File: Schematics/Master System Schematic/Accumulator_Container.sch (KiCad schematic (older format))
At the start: 21 parts, among them J10 Main TS Connector, J11 TSAL Connector, J8 Shutdown/MC Control Connector, J9 TSMP/IMD Connector, K10 SPST-NO (Precharge Control), K11 SPST-NC (Discharge), K12 SPST-NO (AIR Control), K7 SPST-NO (Precharge), K8 SPST-NO (AIR), K9 SPST-NO (AIR), U14 OrionCurrentSens, U7 OrionThermExp

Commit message: Cleaned accumulator
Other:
- moved on the sheet: F6, F7, F8, F9, J10, J11, J9, K11, K7, K8, K9, R2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

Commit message: Revert "Revert "Merge branch 'Dylan_BMS-control-systems-slight-rework' of https://github.com/Northeastern-Electric-Racing/NER into Dylan_BMS-control-systems-slight-rework""
This reverts commit 7bfceb9de4e286d5e46c7b991145f3115c617458.
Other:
- note added: "Contains 4 critical thermistors, 4 critical thermistor gnds, thermistor expansion pwr and gnd, and thermistor expansion CANBUS"
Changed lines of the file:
@@
 Sheet 3 23
 Title "Accumulator Container"
-Date "2020-11-12"
-Rev "6"
+Date "2021-02-08"
+Rev "7"
 Comp "Northeastern Electric Racing"
 Comment1 "https://github.com/Northeastern-Electric-Racing/NER"
@@
 NoConn ~ 2750 1800
 NoConn ~ 4150 1500
-Text HLabel 19650 14600 2    50   Output ~ 0
-Segment1_CriticalThermistors
-Text HLabel 19650 14700 2    50   Output ~ 0
-Segment2_CriticalThermistors
-Text HLabel 19650 14800 2    50   Output ~ 0
-Segment3_CriticalThermistors
-Text HLabel 19650 14900 2    50   Output ~ 0
-Segment4_CriticalThermistors
 Entry Wire Line
 	2350 2300 2250 2400
@@
 	2750 1600 2650 1600
 Text HLabel 19650 13450 2    50   Output ~ 0
-Thermistor_Expansion
+Temperature_Data
 Entry Wire Line
 	2550 1800 2650 1900
@@
 	2650 15900 4150 15900
 Wire Bus Line
-	1300 5150 600  5150
-Wire Bus Line
-	600  5150 600  16400
-Wire Bus Line
-	1300 8050 650  8050
-Wire Bus Line
-	650  8050 650  16300
-Wire Bus Line
-	1300 10950 700  10950
-Wire Bus Line
-	1300 13850 750  13850
-Wire Bus Line
-	750  13850 750  16100
-Wire Bus Line
-	700  10950 700  16200
+	1300 5150 750  5150
+Wire Bus Line
+	1300 8050 700  8050
+Wire Bus Line
+	1300 10950 650  10950
 Wire Bus Line
 	1300 13750 800  13750
@@
 	10100 2150 10100 5600
 Wire Bus Line
-	600  16400 13650 16400
-Wire Bus Line
-	650  16300 13550 16300
-Wire Bus Line
-	700  16200 13450 16200
-Wire Bus Line
-	750  16100 13350 16100
-Wire Bus Line
-	13450 14700 19650 14700
-Wire Bus Line
 	19250 13450 19650 13450
 Wire Bus Line
@@
 Wire Notes Line
 	21100 15000 21100 13350
-Wire Bus Line
-	13650 14900 19650 14900
-Wire Bus Line
-	13550 14800 19650 14800
 Wire Notes Line
 	19450 13350 19450 15000
@@
 Wire Bus Line
 	10600 14300 19650 14300
-Wire Bus Line
-	13350 14600 19650 14600
 Connection ~ 11850 6950
 Wire Wire Line
@@
 	13850 3850 13850 5550
 Wire Bus Line
-	13650 14900 13650 16400
-Wire Bus Line
-	13550 14800 13550 16300
-Wire Bus Line
-	13450 14700 13450 16200
-Wire Bus Line
-	13350 14600 13350 16100
-Wire Bus Line
 	19250 11200 19250 13450
 Wire Bus Line
 	19100 11050 19100 13750
+Entry Bus Bus
+	650  850  750  750
+Wire Bus Line
+	650  10950 650  850
+Wire Bus Line
+	600  13850 600  850
+Wire Bus Line
+	600  13850 1300 13850
+Entry Bus Bus
+	600  850  700  750
+Entry Bus Bus
+	750  850  850  750
+Entry Bus Bus
+	700  850  800  750
+Wire Bus Line
+	700  850  700  8050
+Wire Bus Line
+	750  850  750  5150
 Wire Bus Line
 	10600 12200 10600 14200
@@
 	10700 6400 10700 14000
 Wire Bus Line
-	2650 750  20850 750
-Wire Bus Line
 	10600 14300 10600 15000
 Wire Bus Line
@@
 	18150 6300 20700 6300
 Wire Bus Line
+	700  750  20850 750
+Wire Bus Line
 	4400 3350 4400 4400
 Wire Bus Line
@@
 Wire Bus Line
 	2250 2300 2250 4300
+Text Notes 4500 850  0    50   ~ 0
+Contains 4 critical thermistors, 4 critical thermistor gnds, thermistor expansion pwr and gnd, and thermistor expansion CANBUS
 $EndSCHEMATC

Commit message: Revert "Merge branch 'Dylan_BMS-control-systems-slight-rework' of https://github.com/Northeastern-Electric-Racing/NER into Dylan_BMS-control-systems-slight-rework"
This reverts commit fde7ba4e4a38cad13224d6abfd117b52e4ba179f, reversing
changes made to 479d55be7c023c6502d2d4db07d9957a4b0a3a94.
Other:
- note removed: "Contains 4 critical thermistors, 4 critical thermistor gnds, thermistor expansion pwr and gnd, and thermistor expansion CANBUS"
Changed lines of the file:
@@
 Sheet 3 23
 Title "Accumulator Container"
-Date "2021-02-08"
-Rev "7"
+Date "2020-11-12"
+Rev "6"
 Comp "Northeastern Electric Racing"
 Comment1 "https://github.com/Northeastern-Electric-Racing/NER"
@@
 NoConn ~ 2750 1800
 NoConn ~ 4150 1500
+Text HLabel 19650 14600 2    50   Output ~ 0
+Segment1_CriticalThermistors
+Text HLabel 19650 14700 2    50   Output ~ 0
+Segment2_CriticalThermistors
+Text HLabel 19650 14800 2    50   Output ~ 0
+Segment3_CriticalThermistors
+Text HLabel 19650 14900 2    50   Output ~ 0
+Segment4_CriticalThermistors
 Entry Wire Line
 	2350 2300 2250 2400
@@
 	2750 1600 2650 1600
 Text HLabel 19650 13450 2    50   Output ~ 0
-Temperature_Data
+Thermistor_Expansion
 Entry Wire Line
 	2550 1800 2650 1900
@@
 	2650 15900 4150 15900
 Wire Bus Line
-	1300 5150 750  5150
-Wire Bus Line
-	1300 8050 700  8050
-Wire Bus Line
-	1300 10950 650  10950
+	1300 5150 600  5150
+Wire Bus Line
+	600  5150 600  16400
+Wire Bus Line
+	1300 8050 650  8050
+Wire Bus Line
+	650  8050 650  16300
+Wire Bus Line
+	1300 10950 700  10950
+Wire Bus Line
+	1300 13850 750  13850
+Wire Bus Line
+	750  13850 750  16100
+Wire Bus Line
+	700  10950 700  16200
 Wire Bus Line
 	1300 13750 800  13750
@@
 	10100 2150 10100 5600
 Wire Bus Line
+	600  16400 13650 16400
+Wire Bus Line
+	650  16300 13550 16300
+Wire Bus Line
+	700  16200 13450 16200
+Wire Bus Line
+	750  16100 13350 16100
+Wire Bus Line
+	13450 14700 19650 14700
+Wire Bus Line
 	19250 13450 19650 13450
 Wire Bus Line
@@
 Wire Notes Line
 	21100 15000 21100 13350
+Wire Bus Line
+	13650 14900 19650 14900
+Wire Bus Line
+	13550 14800 19650 14800
 Wire Notes Line
 	19450 13350 19450 15000
@@
 Wire Bus Line
 	10600 14300 19650 14300
+Wire Bus Line
+	13350 14600 19650 14600
 Connection ~ 11850 6950
 Wire Wire Line
@@
 	13850 3850 13850 5550
 Wire Bus Line
+	13650 14900 13650 16400
+Wire Bus Line
+	13550 14800 13550 16300
+Wire Bus Line
+	13450 14700 13450 16200
+Wire Bus Line
+	13350 14600 13350 16100
+Wire Bus Line
 	19250 11200 19250 13450
 Wire Bus Line
 	19100 11050 19100 13750
-Entry Bus Bus
-	650  850  750  750
-Wire Bus Line
-	650  10950 650  850
-Wire Bus Line
-	600  13850 600  850
-Wire Bus Line
-	600  13850 1300 13850
-Entry Bus Bus
-	600  850  700  750
-Entry Bus Bus
-	750  850  850  750
-Entry Bus Bus
-	700  850  800  750
-Wire Bus Line
-	700  850  700  8050
-Wire Bus Line
-	750  850  750  5150
 Wire Bus Line
 	10600 12200 10600 14200
@@
 	10700 6400 10700 14000
 Wire Bus Line
+	2650 750  20850 750
+Wire Bus Line
 	10600 14300 10600 15000
 Wire Bus Line
@@
 	18150 6300 20700 6300
 Wire Bus Line
-	700  750  20850 750
-Wire Bus Line
 	4400 3350 4400 4400
 Wire Bus Line
@@
 Wire Bus Line
 	2250 2300 2250 4300
-Text Notes 4500 850  0    50   ~ 0
-Contains 4 critical thermistors, 4 critical thermistor gnds, thermistor expansion pwr and gnd, and thermistor expansion CANBUS
 $EndSCHEMATC

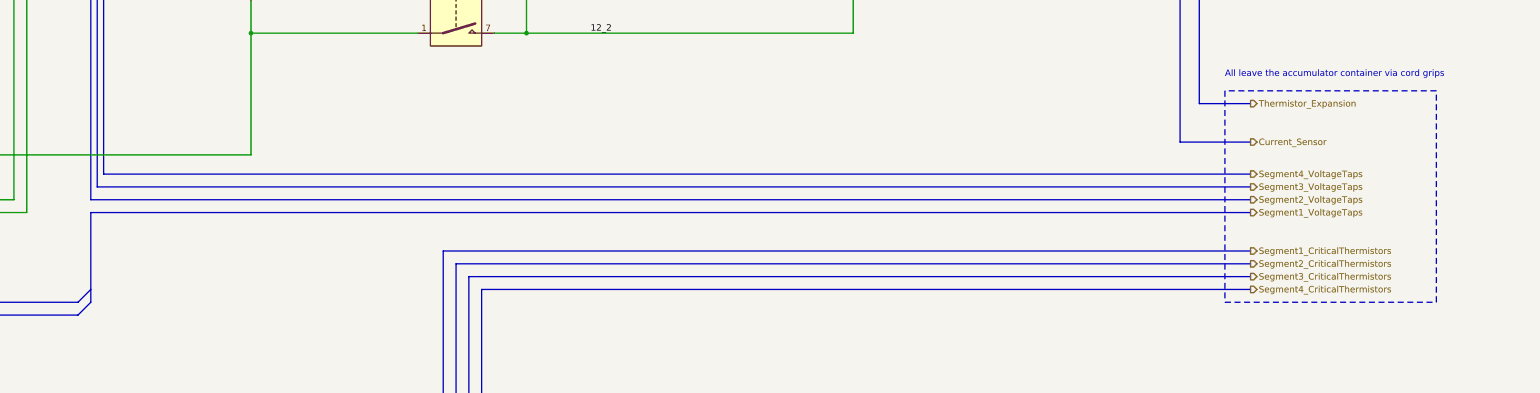
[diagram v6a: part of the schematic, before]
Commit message: Master Schematic and VPM Changes
> Thermal Expansion and Critical Therm busses combined into Temperature_Data in Accumulator_Container.sch
> BattFanPWM added to Temperature_Data connector
> PumpIO connector changed from 2 to 4 pins
> Added 7-Pin Generic connector
> Updated VPM board schematic

VPM Version 5
Master Schematic Version 14.1
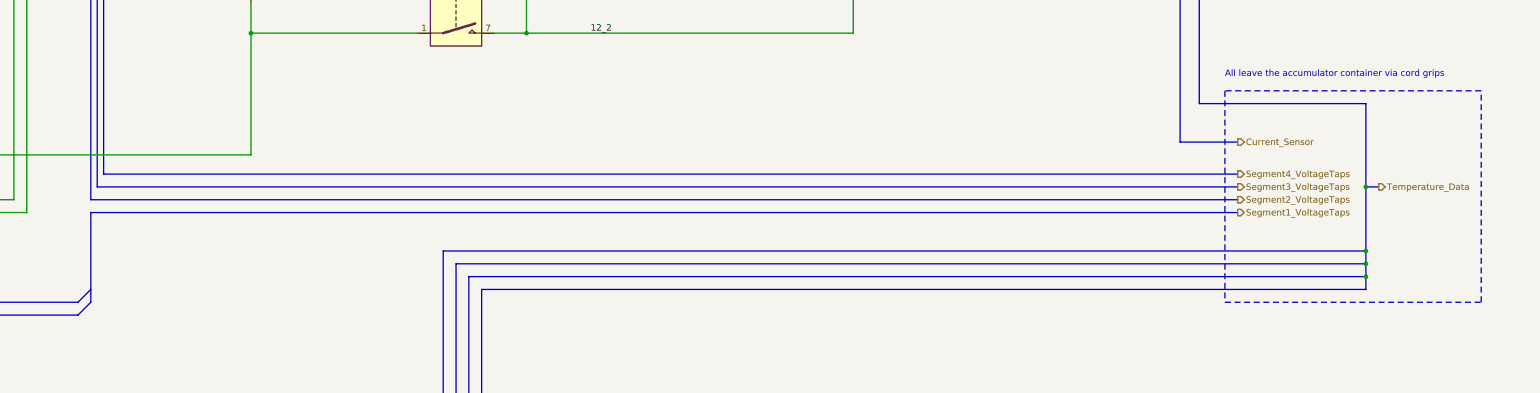
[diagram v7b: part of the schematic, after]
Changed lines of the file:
@@
 Wire Wire Line
 	19300 7050 19650 7050
-Text HLabel 19650 14300 2    50   Output ~ 0
+Text HLabel 19550 14300 2    50   Output ~ 0
 Segment1_VoltageTaps
-Text HLabel 19650 14200 2    50   Output ~ 0
+Text HLabel 19550 14200 2    50   Output ~ 0
 Segment2_VoltageTaps
-Text HLabel 19650 14100 2    50   Output ~ 0
+Text HLabel 19550 14100 2    50   Output ~ 0
 Segment3_VoltageTaps
-Text HLabel 19650 14000 2    50   Output ~ 0
+Text HLabel 19550 14000 2    50   Output ~ 0
 Segment4_VoltageTaps
 $Comp
@@
 Wire Wire Line
 	16550 4350 17850 4350
-$Comp
-L Relay:DIPxx-1Axx-11x K10
-U 1 1 5F80B7CF
-P 13650 3350
-F 0 "K10" V 13083 3350 50  0000 C CNN
-F 1 "SPST-NO (Precharge Control)" V 13174 3350 50  0000 C CNN
-F 2 "Relay_THT:Relay_StandexMeder_DIP_LowProfile" H 14000 3300 50  0001 L CNN
-F 3 "https://standexelectronics.com/wp-content/uploads/datasheet_reed_relay_DIP.pdf" H 13650 3350 50  0001 C CNN
-	1    13650 3350
-	0    1    1    0
-$EndComp
-Wire Wire Line
-	13850 3850 13250 3850
-Wire Wire Line
-	13250 3850 13250 3550
-Wire Wire Line
-	13250 3550 13350 3550
-Wire Wire Line
-	13950 3550 14250 3550
-Wire Wire Line
-	14400 3550 14500 3550
-Wire Wire Line
-	14250 3550 14250 3900
-Wire Wire Line
-	14400 3150 14500 3150
-Wire Wire Line
-	15100 3150 15200 3150
 Wire Wire Line
 	14800 9300 15450 9300
 Wire Wire Line
-	14250 3900 15200 3900
-Wire Wire Line
 	13750 6550 14400 6550
-Wire Notes Line
-	13000 2450 15300 2450
-Wire Notes Line
-	15300 4100 13000 4100
-Wire Wire Line
-	15100 3550 15200 3550
-Wire Wire Line
-	15200 3550 15200 3900
-Connection ~ 15200 3900
-Wire Wire Line
-	15200 3900 15450 3900
-Wire Notes Line
-	15300 4100 15300 2450
-Wire Notes Line
-	13000 2450 13000 4100
-Text Notes 13050 4050 0    50   ~ 0
-MC Control Relay PCB
-$Comp
-L Relay:DIPxx-1Axx-11x K12
-U 1 1 5F814F76
-P 14800 3350
-F 0 "K12" V 14233 3350 50  0000 C CNN
-F 1 "SPST-NO (AIR Control)" V 14324 3350 50  0000 C CNN
-F 2 "Relay_THT:Relay_StandexMeder_DIP_LowProfile" H 15150 3300 50  0001 L CNN
-F 3 "https://standexelectronics.com/wp-content/uploads/datasheet_reed_relay_DIP.pdf" H 14800 3350 50  0001 C CNN
-	1    14800 3350
-	0    1    1    0
-$EndComp
 Text HLabel 6100 10000 2    50   Input ~ 0
 HVD-
@@
 Entry Wire Line
 	18500 6400 18600 6300
-Text HLabel 19650 13750 2    50   Output ~ 0
+Text HLabel 19550 13750 2    50   Output ~ 0
 Current_Sensor
 Wire Wire Line
@@
 	5400 5150 5400 7100
 Wire Wire Line
-	13250 3150 13350 3150
-Wire Wire Line
-	13250 2700 13250 3150
-Wire Wire Line
 	13900 1200 13900 1350
 Wire Wire Line
@@
 MotorController_Precharge+
 Wire Wire Line
-	14250 3150 14250 3550
-Wire Wire Line
-	13950 3150 14250 3150
-Connection ~ 14250 3550
-Wire Wire Line
-	14400 1850 14400 3150
-Wire Wire Line
-	15200 3150 15200 3550
-Connection ~ 15200 3550
-Wire Wire Line
 	14200 2350 15450 2350
 Wire Wire Line
 	12850 2350 14100 2350
-Wire Wire Line
-	13900 1850 13900 2700
-Wire Wire Line
-	13250 2700 13900 2700
 Wire Wire Line
 	14100 1000 14100 1350
@@
 NoConn ~ 2750 1800
 NoConn ~ 4150 1500
-Text HLabel 19650 14600 2    50   Output ~ 0
-Segment1_CriticalThermistors
-Text HLabel 19650 14700 2    50   Output ~ 0
-Segment2_CriticalThermistors
-Text HLabel 19650 14800 2    50   Output ~ 0
-Segment3_CriticalThermistors
-Text HLabel 19650 14900 2    50   Output ~ 0
-Segment4_CriticalThermistors
 Entry Wire Line
 	2350 2300 2250 2400
@@
 Wire Wire Line
 	2750 1600 2650 1600
-Text HLabel 19650 13450 2    50   Output ~ 0
-Thermistor_Expansion
+Text HLabel 20650 14100 2    50   Output ~ 0
+Temperature_Data
 Entry Wire Line
 	2550 1800 2650 1900
@@
 	2550 850  2650 750
 Wire Notes Line
-	19450 15000 21100 15000
+	19450 15000 21450 15000
 Wire Notes Line
-	21100 13350 19450 13350
+	21450 13350 19450 13350
 Text Notes 19450 13250 0    50   ~ 0
 All leave the accumulator container via cord grips
@@
 	750  16100 13350 16100
 Wire Bus Line
-	13450 14700 19650 14700
-Wire Bus Line
-	19250 13450 19650 13450
-Wire Bus Line
-	19100 13750 19650 13750
+	19100 13750 19550 13750
 Entry Bus Bus
 	10600 6300 10700 6400
@@
 	8050 6300 10600 6300
 Wire Notes Line
-	21100 15000 21100 13350
-Wire Bus Line
-	13650 14900 19650 14900
-Wire Bus Line
-	13550 14800 19650 14800
+	21450 15000 21450 13350
 Wire Notes Line
 	19450 13350 19450 15000
@@
 	17600 10900 11850 10900
 Wire Bus Line
-	10700 14000 19650 14000
-Wire Bus Line
-	10650 14100 19650 14100
-Wire Bus Line
-	10600 14200 19650 14200
-Wire Bus Line
-	10600 14300 19650 14300
-Wire Bus Line
-	13350 14600 19650 14600
+	10700 14000 19550 14000
+Wire Bus Line
+	10650 14100 19550 14100
+Wire Bus Line
+	10600 14200 19550 14200
+Wire Bus Line
+	10600 14300 19550 14300
 Connection ~ 11850 6950
+Wire Wire Line
+	11850 5050 11850 5950
+Wire Wire Line
+	13750 12900 14000 12900
+Wire Wire Line
+	5250 13850 11850 13850
+Wire Wire Line
+	11850 12650 11850 12900
+Wire Wire Line
+	11850 12900 13150 12900
+Connection ~ 11850 12900
+Wire Wire Line
+	11850 12900 11850 13850
+Connection ~ 14000 12900
+Wire Wire Line
+	14000 12900 16550 12900
+Wire Bus Line
+	20700 6300 20700 11050
+Connection ~ 12850 5550
+Wire Wire Line
+	12850 2350 12850 5550
+Connection ~ 15450 9300
+Wire Bus Line
+	13650 14900 13650 16400
+Wire Bus Line
+	13550 14800 13550 16300
+Wire Bus Line
+	13450 14700 13450 16200
+Wire Bus Line
+	13350 14600 13350 16100
+Wire Bus Line
+	19250 11200 19250 13450
+Wire Bus Line
+	19100 11050 19100 13750
+Wire Bus Line
+	20550 13450 20550 14100
+Wire Bus Line
+	19250 13450 20550 13450
+Wire Bus Line
+	13350 14600 20550 14600
+Wire Bus Line
+	20550 14700 20550 14600
+Wire Bus Line
+	13450 14700 20550 14700
+Connection ~ 20550 14600
+Wire Bus Line
+	20550 14800 20550 14700
+Wire Bus Line
+	13550 14800 20550 14800
+Connection ~ 20550 14700
+Wire Bus Line
+	20550 14900 20550 14800
+Connection ~ 20550 14800
+Wire Bus Line
+	13650 14900 20550 14900
+Wire Bus Line
+	20650 14100 20550 14100
+Connection ~ 20550 14100
+Wire Bus Line
+	20550 14100 20550 14600
+Wire Wire Line
+	13850 3850 13850 5550
+Wire Wire Line
+	14400 6550 14400 3550
+Wire Wire Line
+	13250 2700 13900 2700
+Wire Wire Line
+	13900 1850 13900 2700
+Wire Wire Line
+	14400 1850 14400 3150
+Wire Wire Line
+	13950 3150 14250 3150
+Wire Wire Line
+	13250 2700 13250 3150
+Wire Wire Line
+	13250 3150 13350 3150
+$Comp
+L Relay:DIPxx-1Axx-11x K12
+U 1 1 5F814F76
+P 14800 3350
+F 0 "K12" V 14233 3350 50  0000 C CNN
+F 1 "SPST-NO (AIR Control)" V 14324 3350 50  0000 C CNN
+F 2 "Relay_THT:Relay_StandexMeder_DIP_LowProfile" H 15150 3300 50  0001 L CNN
+F 3 "https://standexelectronics.com/wp-content/uploads/datasheet_reed_relay_DIP.pdf" H 14800 3350 50  0001 C CNN
+	1    14800 3350
+	0    1    1    0
+$EndComp
+Text Notes 13050 4050 0    50   ~ 0
+MC Control Relay PCB
+Wire Notes Line
+	13000 2450 13000 4100
+Wire Notes Line
+	15300 4100 15300 2450
+Wire Wire Line
+	15450 3900 15450 9300
 Wire Wire Line
 	15450 2350 15450 3900
 Connection ~ 15450 3900
 Wire Wire Line
-	11850 5050 11850 5950
-Wire Wire Line
-	13750 12900 14000 12900
-Wire Wire Line
-	5250 13850 11850 13850
-Wire Wire Line
-	11850 12650 11850 12900
-Wire Wire Line
-	11850 12900 13150 12900
-Connection ~ 11850 12900
-Wire Wire Line
-	11850 12900 11850 13850
-Connection ~ 14000 12900
-Wire Wire Line
-	14000 12900 16550 12900
-Wire Bus Line
-	20700 6300 20700 11050
-Connection ~ 12850 5550
-Wire Wire Line
-	12850 2350 12850 5550
-Wire Wire Line
-	15450 3900 15450 9300
-Connection ~ 15450 9300
-Wire Wire Line
-	14400 6550 14400 3550
-Wire Wire Line
-	13850 3850 13850 5550
-Wire Bus Line
-	13650 14900 13650 16400
-Wire Bus Line
-	13550 14800 13550 16300
-Wire Bus Line
-	13450 14700 13450 16200
-Wire Bus Line
-	13350 14600 13350 16100
-Wire Bus Line
-	19250 11200 19250 13450
-Wire Bus Line
-	19100 11050 19100 13750
+	15200 3900 15450 3900
+Wire Wire Line
+	15200 3150 15200 3550
+Wire Wire Line
+	15200 3550 15200 3900
+Connection ~ 15200 3550
+Wire Wire Line
+	15100 3550 15200 3550
+Wire Notes Line
+	15300 4100 13000 4100
+Wire Notes Line
+	13000 2450 15300 2450
+Connection ~ 15200 3900
+Wire Wire Line
+	14250 3900 15200 3900
+Wire Wire Line
+	15100 3150 15200 3150
+Wire Wire Line
+	14400 3150 14500 3150
+Wire Wire Line
+	14400 3550 14500 3550
+Wire Wire Line
+	14250 3150 14250 3550
+Wire Wire Line
+	14250 3550 14250 3900
+Connection ~ 14250 3550
+Wire Wire Line
+	13950 3550 14250 3550
+Wire Wire Line
+	13250 3550 13350 3550
+Wire Wire Line
+	13250 3850 13250 3550
+Wire Wire Line
+	13850 3850 13250 3850
+$Comp
+L Relay:DIPxx-1Axx-11x K10
+U 1 1 5F80B7CF
+P 13650 3350
+F 0 "K10" V 13083 3350 50  0000 C CNN
+F 1 "SPST-NO (Precharge Control)" V 13174 3350 50  0000 C CNN
+F 2 "Relay_THT:Relay_StandexMeder_DIP_LowProfile" H 14000 3300 50  0001 L CNN
+F 3 "https://standexelectronics.com/wp-content/uploads/datasheet_reed_relay_DIP.pdf" H 13650 3350 50  0001 C CNN
+	1    13650 3350
+	0    1    1    0
+$EndComp
+Wire Bus Line
+	10600 14300 10600 15000
 Wire Bus Line
 	10600 12200 10600 14200
@@
 	2650 750  20850 750
 Wire Bus Line
-	10600 14300 10600 15000
-Wire Bus Line
 	2550 850  2550 1800
